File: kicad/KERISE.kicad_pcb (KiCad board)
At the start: 2 copper layers, 34 x 44 mm, 88 parts, among them J1 Motor_L, J10 ENC_Slave, J11 ENC_Host, J12 ENC_Slave, J13 Host, J14 Slave, J15 Host, J16 Slave, J2 Motor_R, J3 Host, J4 Slave, J5 Host, J6 Slave, J7 COM, J8 Fan, J9 ENC_Host, Q1 MTM231232LBF, Q10 SFH3015FA, Q11 MTM231232LBF, Q12 DMN3065LW-7, Q13 SFH3015FA, Q14 DMN3065LW-7, Q2 DMN3065LW-7, Q3 SFH3015FA, Q4 MTM231232LBF, Q5 DMN3065LW-7, Q6 SFH3015FA, Q7 DMN3065LW-7, Q8 MTM231232LBF, Q9 DMN3065LW-7, SW1 RESET, SW2 UPLOAD, U1 ESP32-PICO-D4, U2 DRV8835, U3 LXDC2UR30, U4 MA702, U5 MA702, U6 ICM-20602, U7 ICM-20602, U8 PCA9632

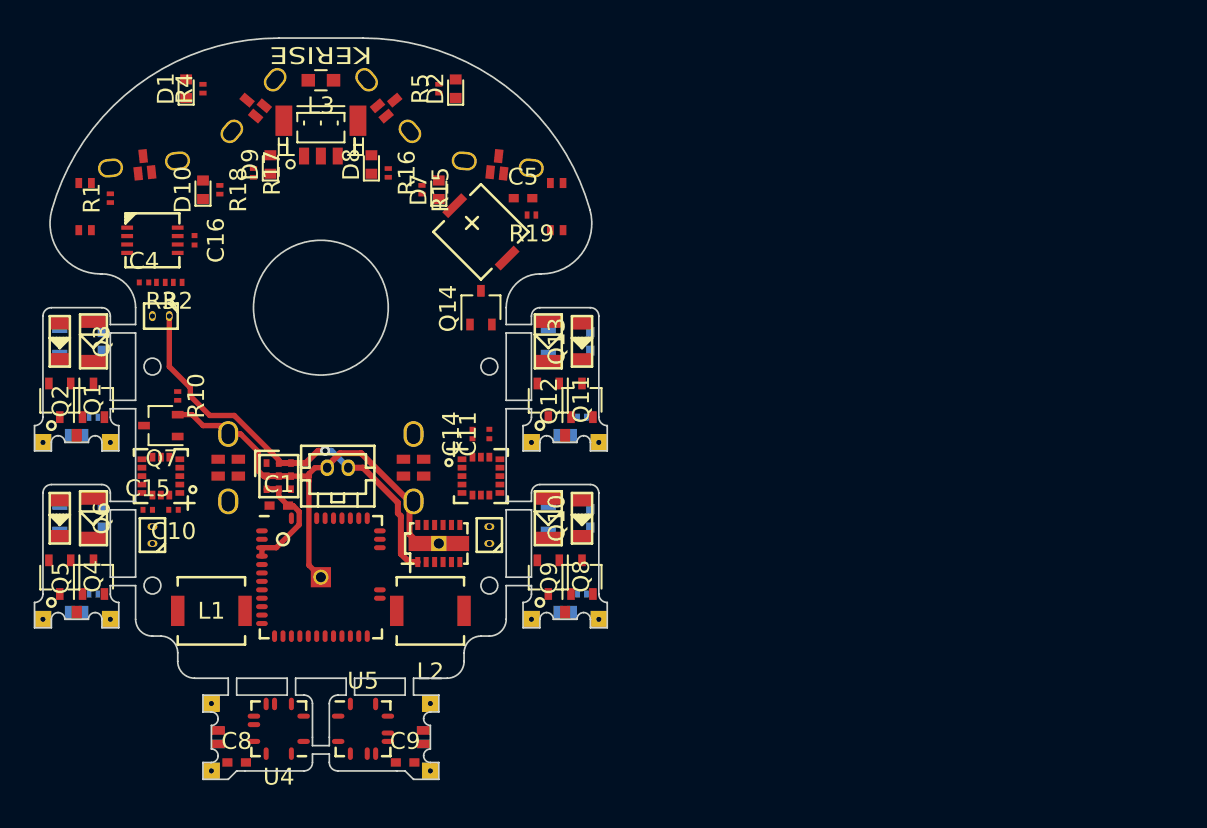
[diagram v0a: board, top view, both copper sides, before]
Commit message: 自動配線あと4本
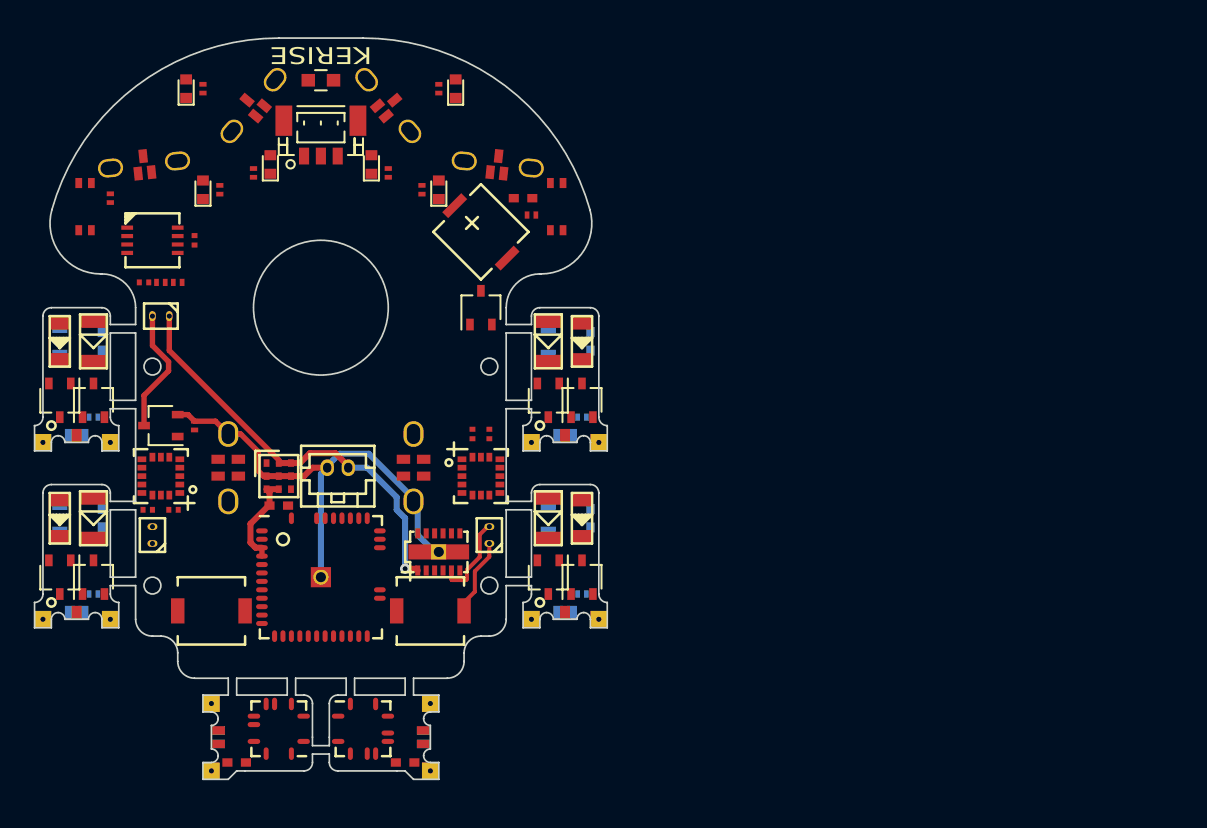
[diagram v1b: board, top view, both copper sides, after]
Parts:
- added G***: LOGO, mouse:KERI_9mm, B.Cu at (148.5, 115.8)
- moved R10 2.02 mm to (141.0, 110.0), turned to 90 degrees
- moved U2 0.50 mm to (155.5, 117.5)
- turned C1 to 180 degrees
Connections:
- U1 pad 15: (no net) -> SPI-CS-IMU_L
- U1 pad 16: (no net) -> SPI-CS-IMU_R
- U6 pad 5: (no net) -> SPI-CS-IMU_R
- U7 pad 5: (no net) -> SPI-CS-IMU_L
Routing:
- net /Fan/fan_to_fet: track 0.00 -> 7.50 mm
- net /Motor/MT_OUT_R2: track 0.00 -> 5.22 mm
- net /Motor/MT_OUT_R1: track 0.00 -> 4.62 mm
- net GND: track 30.4 -> 28.5 mm
- net +3V3: track 6.79 -> 5.77 mm
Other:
- board text added: "2018.09.06"

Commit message: 自動配線4本Take2
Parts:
- moved C9 3.50 mm to (153.4, 126.5)
- moved C8 3.50 mm to (143.5, 126.5)
- turned C4 to 90 degrees
- turned J2 to 270 degrees
- turned R2 to 90 degrees
- turned R3 to 90 degrees
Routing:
- net GND: track 28.5 -> 26.5 mm
- net /Motor/MT_OUT_R1: track 4.62 -> 6.15 mm
- net /Motor/MT_OUT_R2: track 5.22 -> 4.16 mm
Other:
- outline, holes or cut-outs redrawn

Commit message: 手動配線
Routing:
- net +3V3: track 5.77 -> 136.7 mm, vias 0 -> 3
- net GND: track 26.5 -> 151.9 mm, vias 0 -> 3
- net PR-LED-SL: track 0.00 -> 65.3 mm, vias 0 -> 2
- net VDDA: track 0.00 -> 62.8 mm, vias 0 -> 2
- net PR-LED-SR: track 0.00 -> 51.0 mm, vias 0 -> 2
- net PR-RCV-SL: track 0.00 -> 47.5 mm, vias 0 -> 2
- net PR-LED-FR: track 0.00 -> 47.2 mm, vias 0 -> 4
- net SPI-SCLK: track 0.00 -> 43.5 mm, vias 0 -> 4
- net (no net): track 0.00 -> 40.0 mm, vias 0 -> 2
- net PR-LED-FL: track 0.00 -> 39.8 mm, vias 0 -> 2
- net PR-RCV-FR: track 0.00 -> 37.5 mm, vias 0 -> 2
- net SPI-MOSI: track 0.00 -> 37.5 mm, vias 0 -> 2
- net SPEAKER: track 0.00 -> 35.8 mm, vias 0 -> 4
- net PR-RCV-SR: track 0.00 -> 35.7 mm, vias 0 -> 4
- net I2C-SDA: track 0.00 -> 32.0 mm, vias 0 -> 4
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
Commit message: コンデンサを追加
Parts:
- added C5: 47u, Capacitors_SMD:C_0805, F.Cu at (142.0, 116.5)
- moved G*** 19.2 mm to (148.5, 96.5)
- renumbered C9 to C10, C10 to C11, C11 to C12, C12 to C13, C13 to C14, C14 to C15, C15 to C16, C16 to C17, C5 to C6, C6 to C7, C7 to C8, C8 to C9
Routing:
- net GND: track 151.9 -> 161.0 mm
- net +3V3: track 136.7 -> 141.2 mm
- net PR-RCV-SL: track 47.5 -> 48.5 mm
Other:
- board text added: "2018.09.08"
- board text removed: "2018.09.06"

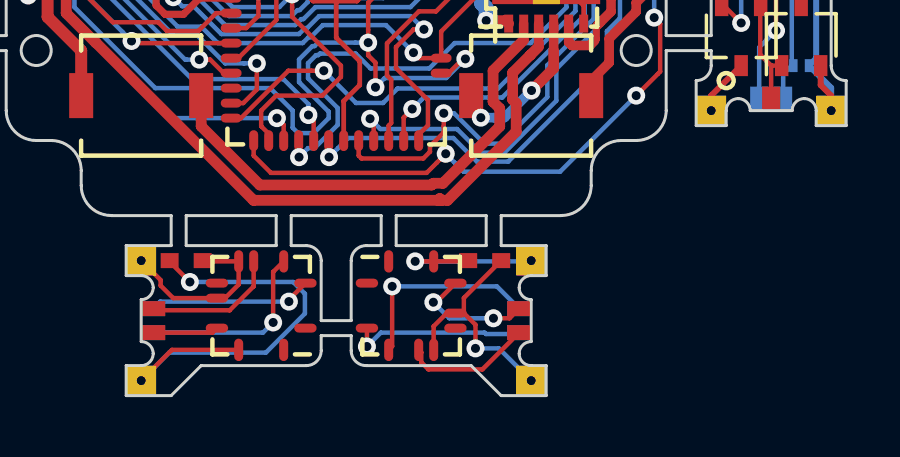
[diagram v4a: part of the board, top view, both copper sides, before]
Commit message: 配線を修正
- エンコーダの配線が基板外に出てた（Elecrowから指摘）
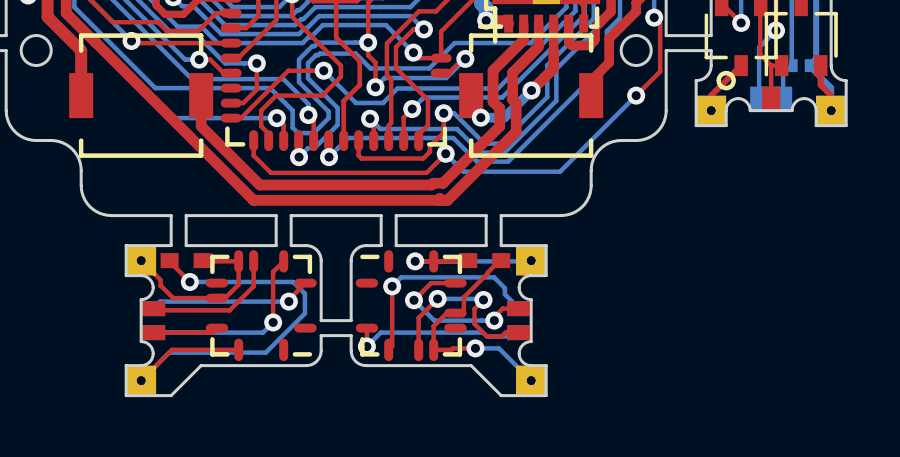
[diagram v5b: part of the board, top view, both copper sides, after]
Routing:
- net /Encoder_L/s_MISO: track 4.32 -> 6.14 mm, vias 0 -> 2
- net /Encoder_L/s_SCLK: track 4.22 -> 5.64 mm
- net /Encoder_L/s_GND: track 7.88 -> 8.52 mm
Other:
- board text added: "2018.09.15"
- board text removed: "2018.09.08"

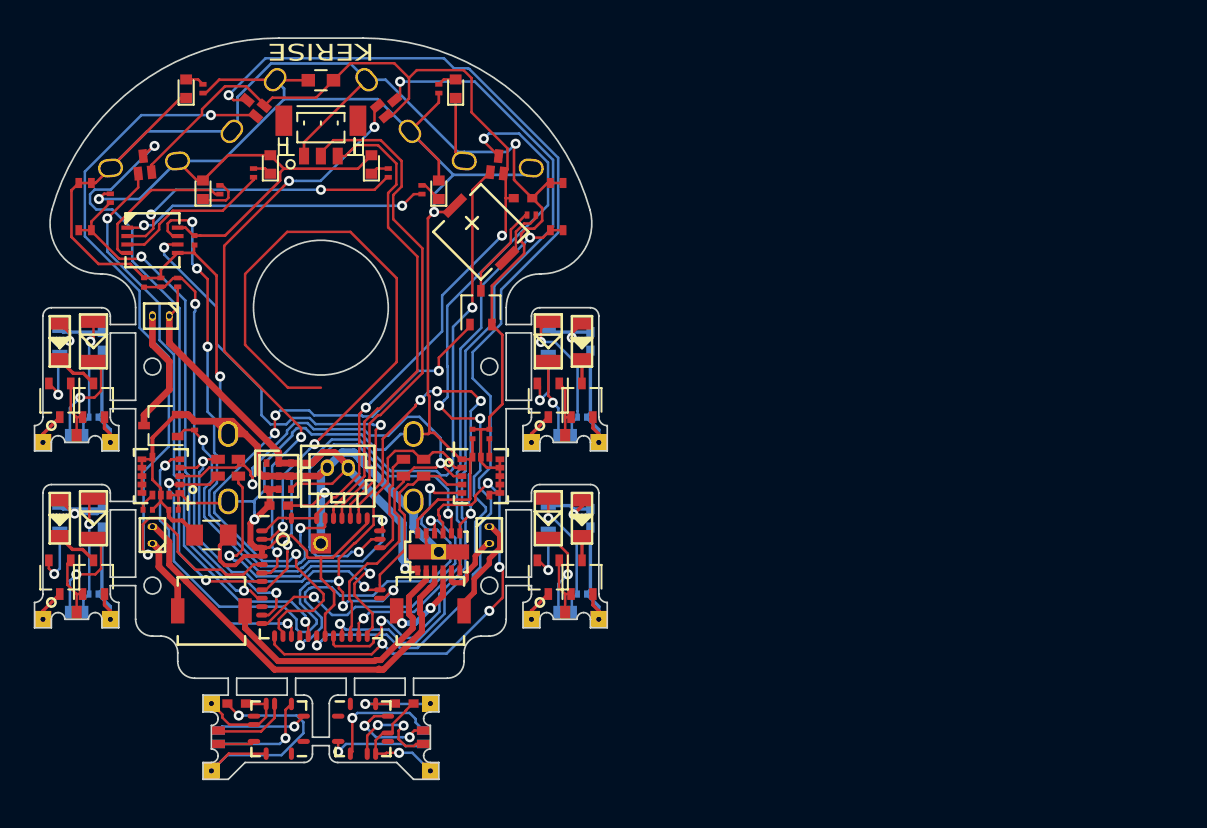
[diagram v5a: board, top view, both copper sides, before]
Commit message: フットプリントを割り当て
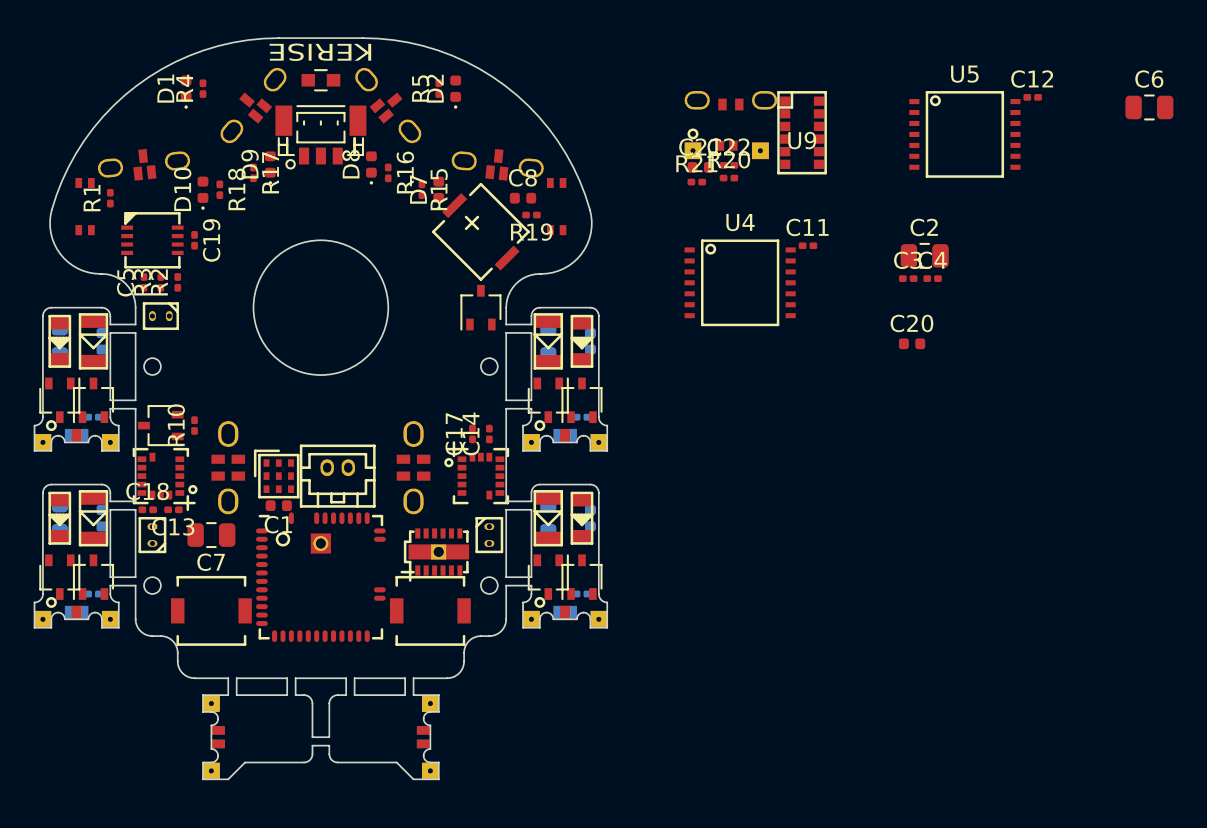
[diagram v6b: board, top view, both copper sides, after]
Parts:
- removed G***: LOGO, mouse:KERI_9mm
- added C18: 0.1u, Capacitor_SMD:C_0201_0603Metric, F.Cu at (138.2, 115.0)
- added C19: 0.1u, Capacitor_SMD:C_0201_0603Metric, F.Cu at (141.0, 99.0)
- added C2: 47u, Capacitor_SMD:C_0805_2012Metric, F.Cu at (184.3, 99.9)
- added C20: 10u, Capacitor_SMD:C_0402_1005Metric, F.Cu at (183.6, 105.1)
- added C21: 4.7u, Capacitor_SMD:C_0402_1005Metric, F.Cu at (171.0, 94.7)
- added C22: 0.1u, Capacitor_SMD:C_0201_0603Metric, F.Cu at (172.7, 94.6)
- added C3: 0.1u, Capacitor_SMD:C_0201_0603Metric, F.Cu at (183.4, 101.3)
- added P1: ToF_Host, mouse:STAND_HOST_04, F.Cu at (172.8, 90.7)
- added P2: ToF_Slave, mouse:STAND_SLAVE_04, F.Cu at (172.6, 93.7)
- added R20: 4.7k, Resistor_SMD:R_0201_0603Metric, F.Cu at (172.7, 95.3)
- added R21: 4.7k, Resistor_SMD:R_0201_0603Metric, F.Cu at (170.8, 95.5)
- added U9: VL6180X, mouse:VL6180X, F.Cu at (177.1, 92.6)
- C1: footprint Capacitors_SMD:C_0402_NoSilk -> Capacitor_SMD:C_0402_1005Metric
- C10, C9: footprint Capacitors_SMD:C_0402_NoSilk -> Capacitor_SMD:C_0402_1005Metric; moved to B.Cu
- C11, C12, C17, C4: footprint Capacitors_SMD:C_0201_NoSilk -> Capacitor_SMD:C_0201_0603Metric
- C13, C14: value 1u -> 0.1u; footprint Capacitors_SMD:C_0402_NoSilk -> Capacitor_SMD:C_0201_0603Metric; moved to F.Cu
- C15, C16: value 0.1u -> 1u; footprint Capacitors_SMD:C_0201_NoSilk -> Capacitor_SMD:C_0402_1005Metric; moved to B.Cu
- C5: value 47u -> 0.1u; footprint Capacitors_SMD:C_0805 -> Capacitor_SMD:C_0201_0603Metric
- C6: value 10u -> 47u; footprint Capacitors_SMD:C_0402_NoSilk -> Capacitor_SMD:C_0805_2012Metric
- C7: value 1u -> 47u; footprint Capacitors_SMD:C_0402_NoSilk -> Capacitor_SMD:C_0805_2012Metric; moved to F.Cu
- C8: value 1u -> 10u; footprint Capacitors_SMD:C_0402_NoSilk -> Capacitor_SMD:C_0402_1005Metric; moved to F.Cu
- D1, D10, D2, D7, D8, D9: footprint LEDs:LED_0402 -> LED_SMD:LED_0402_1005Metric
- R1, R10, R12, R14, R15, R16, R17, R18, R19, R2, R3, R4, R5, R7, R9: footprint Resistors_SMD:R_0201_NoSilk -> Resistor_SMD:R_0201_0603Metric
- R11, R13, R6, R8: footprint Resistors_SMD:R_0603 -> Resistor_SMD:R_0603_1608Metric
- U4, U5: value MA702 -> AS5048A; footprint mouse:MA702 -> mouse:TSSOP-14_4.4x5mm_Pitch0.65mm
- moved U5 50.2 mm to (186.7, 92.7)
- moved C4 46.8 mm to (184.8, 101.3), turned to 0 degrees
- moved C11 40.8 mm to (177.4, 99.3), turned to 0 degrees
- moved U4 38.1 mm to (173.4, 101.5), turned to 0 degrees
- moved C12 37.9 mm to (190.8, 90.5), turned to 0 degrees
- moved C6 37.6 mm to (197.7, 91.1)
- moved C8 31.4 mm to (160.5, 96.5), turned to 0 degrees
- moved C16 28.1 mm to (164.5, 105.0), turned to 270 degrees
- moved C13 24.8 mm to (139.8, 115.0), turned to 180 degrees
- moved C9 22.9 mm to (135.5, 105.0), turned to 270 degrees
- moved C10 21.1 mm to (135.5, 115.5), turned to 270 degrees
- moved C17 20.1 mm to (157.5, 110.5), turned to 90 degrees
- moved C5 15.5 mm to (138.0, 101.5), turned to 90 degrees
- moved C7 13.2 mm to (142.0, 116.5), turned to 180 degrees
- moved C15 8.60 mm to (164.5, 115.5), turned to 270 degrees
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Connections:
- C10 pad 1: /Encoder_L/s_VDD -> /IR_RCV_SR/LED_to_C
- C10 pad 2: /Encoder_L/s_GND -> /IR_RCV_SR/s_GND
- C11 pad 1: +3V3 -> /Encoder_R/s_VDD
- C11 pad 2: GND -> /Encoder_R/s_GND
- C12 pad 1: Net-(C12-Pad1) -> /Encoder_L/s_VDD
- C12 pad 2: GND -> /Encoder_L/s_GND
- C13 pad 1: /IR_RCV_FL/LED_to_C -> +3V3
- C13 pad 2: /IR_RCV_FL/s_GND -> GND
- C14 pad 1: /IR_RCV_FR/LED_to_C -> Net-(C14-Pad1)
- C14 pad 2: /IR_RCV_FR/s_GND -> GND
- C15 pad 1: +3V3 -> /IR_RCV_FL/LED_to_C
- C15 pad 2: GND -> /IR_RCV_FL/s_GND
- C16 pad 1: Net-(C16-Pad1) -> /IR_RCV_FR/LED_to_C
- C16 pad 2: GND -> /IR_RCV_FR/s_GND
- C4 pad 1: BAT-VOL -> +3V3
- C5 pad 1: +3V3 -> BAT-VOL
- C6 pad 1: VDDA -> +BATT
- C7 pad 1: /IR_RCV_SL/LED_to_C -> +3V3
- C7 pad 2: /IR_RCV_SL/s_GND -> GND
- C8 pad 1: /IR_RCV_SR/LED_to_C -> VDDA
- C8 pad 2: /IR_RCV_SR/s_GND -> GND
- C9 pad 1: /Encoder_R/s_VDD -> /IR_RCV_SL/LED_to_C
- C9 pad 2: /Encoder_R/s_GND -> /IR_RCV_SL/s_GND
- J11 pad 2: SPI-CS-ENC_L -> SPI-CS-ENC
- J11 pad 4: SPI-MOSI -> ENC-CHAIN
- J9 pad 2: SPI-CS-ENC_R -> SPI-CS-ENC
- J9 pad 5: SPI-MISO -> ENC-CHAIN
- LS1 pad 1: +3V3 -> +BATT
- U1 pad 24: SPI-CS-ENC_L -> SPI-CS-ENC
- U4 pad 1: (no net) -> /Encoder_R/s_CS
- U4 pad 12: /Encoder_R/s_SCLK -> /Encoder_R/s_VDD
- U4 pad 13: /Encoder_R/s_VDD -> /Encoder_R/s_GND
- U4 pad 5: /Encoder_R/s_CS -> /Encoder_R/s_GND
- U4 pad 7: /Encoder_R/s_MISO -> /Encoder_R/s_GND
- U4 pad 9: (no net) -> /Encoder_R/s_GND
- U5 pad 1: (no net) -> /Encoder_L/s_CS
- U5 pad 12: /Encoder_L/s_SCLK -> /Encoder_L/s_VDD
- U5 pad 13: /Encoder_L/s_VDD -> /Encoder_L/s_GND
- U5 pad 5: /Encoder_L/s_CS -> /Encoder_L/s_GND
- U5 pad 7: /Encoder_L/s_MISO -> /Encoder_L/s_GND
- U5 pad 9: (no net) -> /Encoder_L/s_GND
- U6 pad 14: Net-(C12-Pad1) -> Net-(C14-Pad1)
- U7 pad 14: Net-(C16-Pad1) -> Net-(C18-Pad1)
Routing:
- net GND: track 161.0 -> 0.00 mm, vias 3 -> 0
- net +3V3: track 141.2 -> 0.00 mm, vias 3 -> 0
- net PR-LED-SL: track 65.3 -> 0.00 mm, vias 2 -> 0
- net VDDA: track 62.8 -> 0.00 mm, vias 2 -> 0
- net PR-LED-SR: track 51.0 -> 0.00 mm, vias 2 -> 0
- net PR-RCV-SL: track 48.5 -> 0.00 mm, vias 2 -> 0
- net PR-LED-FR: track 47.2 -> 0.00 mm, vias 4 -> 0
- net SPI-SCLK: track 43.5 -> 0.00 mm, vias 4 -> 0
- net (no net): track 40.0 -> 0.00 mm, vias 2 -> 0
- net PR-LED-FL: track 39.9 -> 0.00 mm, vias 2 -> 0
- net PR-RCV-FR: track 37.5 -> 0.00 mm, vias 2 -> 0
- net SPI-MOSI: track 37.5 -> 0.00 mm, vias 2 -> 0
- net PR-RCV-SR: track 36.0 -> 0.00 mm, vias 4 -> 0
- net SPEAKER: track 35.8 -> 0.00 mm, vias 4 -> 0
- net I2C-SDA: track 32.0 -> 0.00 mm, vias 4 -> 0
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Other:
- board text added: "2019.01.01"
- board text removed: "2018.09.15"

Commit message: 部品を配置
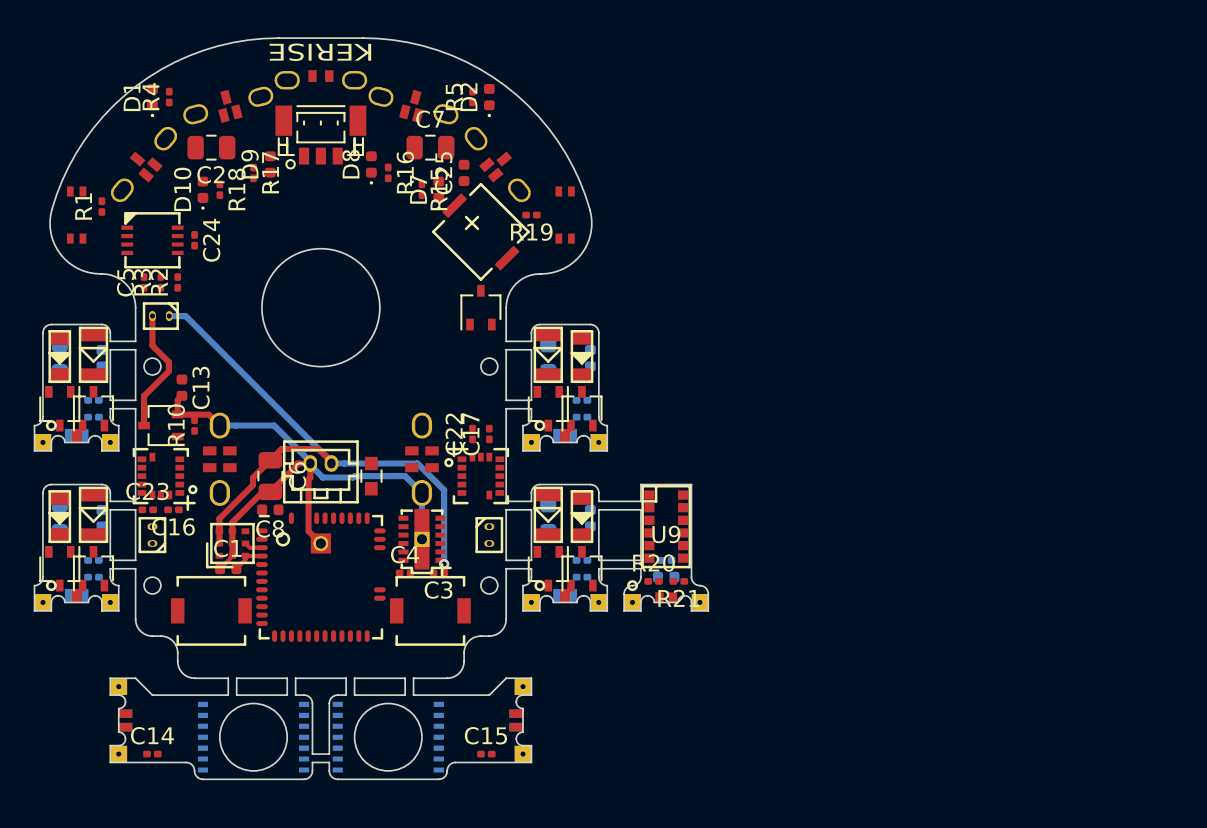
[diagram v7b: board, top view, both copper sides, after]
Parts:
- removed the C16 at (164.5, 105.0)
- added C10: 0.1u, Capacitor_SMD:C_0201_0603Metric, B.Cu at (135.0, 108.5)
- added C12: 0.1u, Capacitor_SMD:C_0201_0603Metric, B.Cu at (135.0, 118.0)
- added C13: 10u, Capacitor_SMD:C_0402_1005Metric, F.Cu at (140.2, 107.8)
- added C19: 0.1u, Capacitor_SMD:C_0201_0603Metric, B.Cu at (164.0, 118.0)
- added C21: 0.1u, Capacitor_SMD:C_0201_0603Metric, B.Cu at (164.0, 108.5)
- added C25: 10u, Capacitor_SMD:C_0402_1005Metric, F.Cu at (157.0, 95.0)
- C20: value 10u -> 1u; moved to B.Cu
- C26: renamed from C21; moved to B.Cu
- C27: renamed from C22; moved to B.Cu
- U4, U5: moved to B.Cu
- moved C6 56.6 mm to (145.5, 113.0), turned to 270 degrees
- moved C15 50.7 mm to (158.3, 129.5)
- moved U5 49.5 mm to (152.5, 128.5), turned to 180 degrees
- moved C14 49.2 mm to (138.5, 129.5)
- moved C2 42.8 mm to (142.0, 93.5), turned to 180 degrees
- moved U4 39.5 mm to (144.5, 128.5)
- moved C4 35.9 mm to (153.5, 118.8)
- moved C3 32.9 mm to (155.5, 118.8), turned to 180 degrees
- moved P2 27.1 mm to (169.0, 120.5)
- moved C7 26.4 mm to (155.0, 93.5), turned to 0 degrees
- moved U9 24.7 mm to (169.0, 116.0)
- moved C26 24.4 mm to (169.0, 119.0)
- moved P1 24.4 mm to (148.5, 89.5), turned to 180 degrees
- moved R20 24.4 mm to (168.2, 119.2)
- moved C8 23.8 mm to (145.5, 115.0), turned to 180 degrees
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- renumbered C10 to C11, C11 to C14, C12 to C15, C13 to C16, C14 to C17, C15 to C18, C17 to C22, C18 to C23, C19 to C24
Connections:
- C20 pad 1: +BATT -> /IR_RCV_FR/LED_to_C
- C20 pad 2: GND -> /IR_RCV_FR/s_GND
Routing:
- net +BATT: track 0.00 -> 36.7 mm, vias 0 -> 1
- net GND: track 0.00 -> 35.4 mm
- net /Fan/fan_to_fet: track 0.00 -> 7.51 mm
- net +3V3: track 0.00 -> 3.06 mm
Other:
- board size 34 x 44 mm -> 40 x 44 mm
